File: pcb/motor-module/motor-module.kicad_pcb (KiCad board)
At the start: 2 copper layers, 37 x 27 mm, 9 parts, among them J1 Connector_male, J2 Screw_Terminal_01x02, K1 AZ822-2C-5DSE Signal-Relais, 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, Q1 2N 2222A SMD Bipolartransisto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

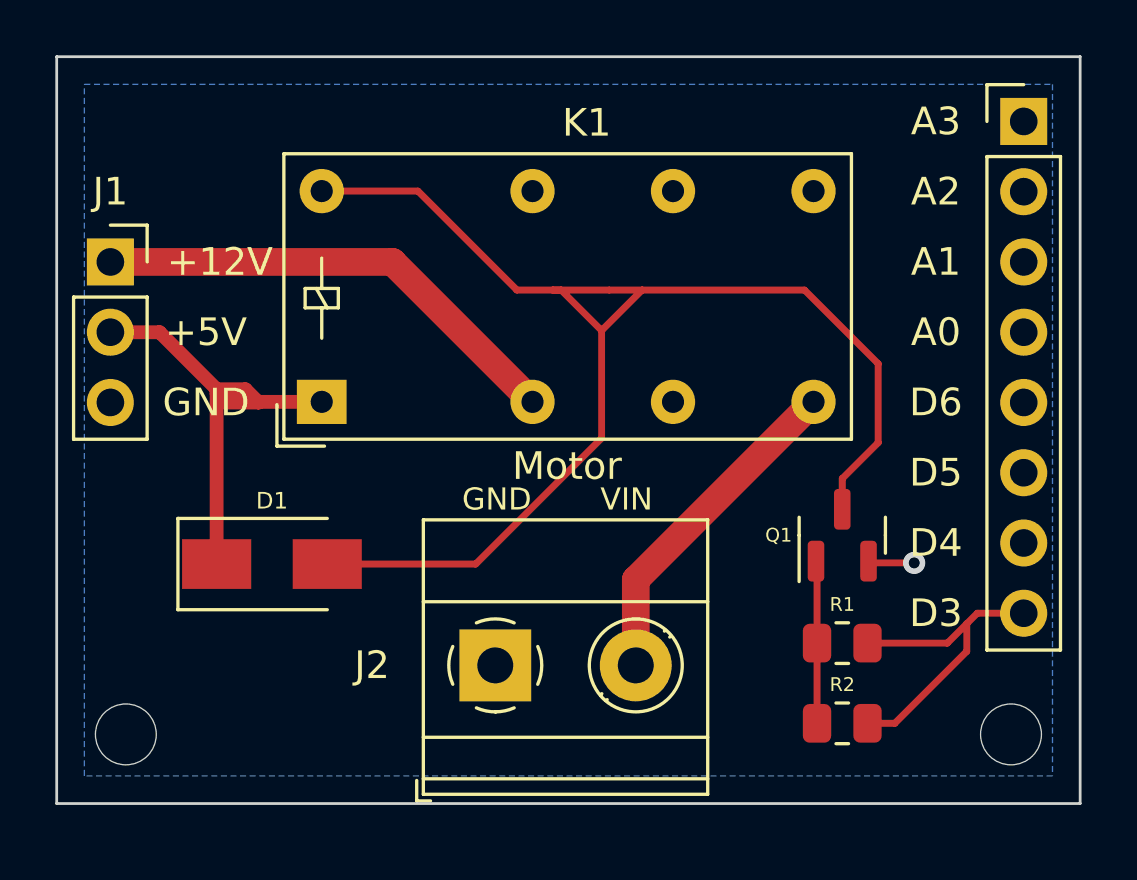
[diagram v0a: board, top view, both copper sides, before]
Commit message: added AVRISP adapter to pcb
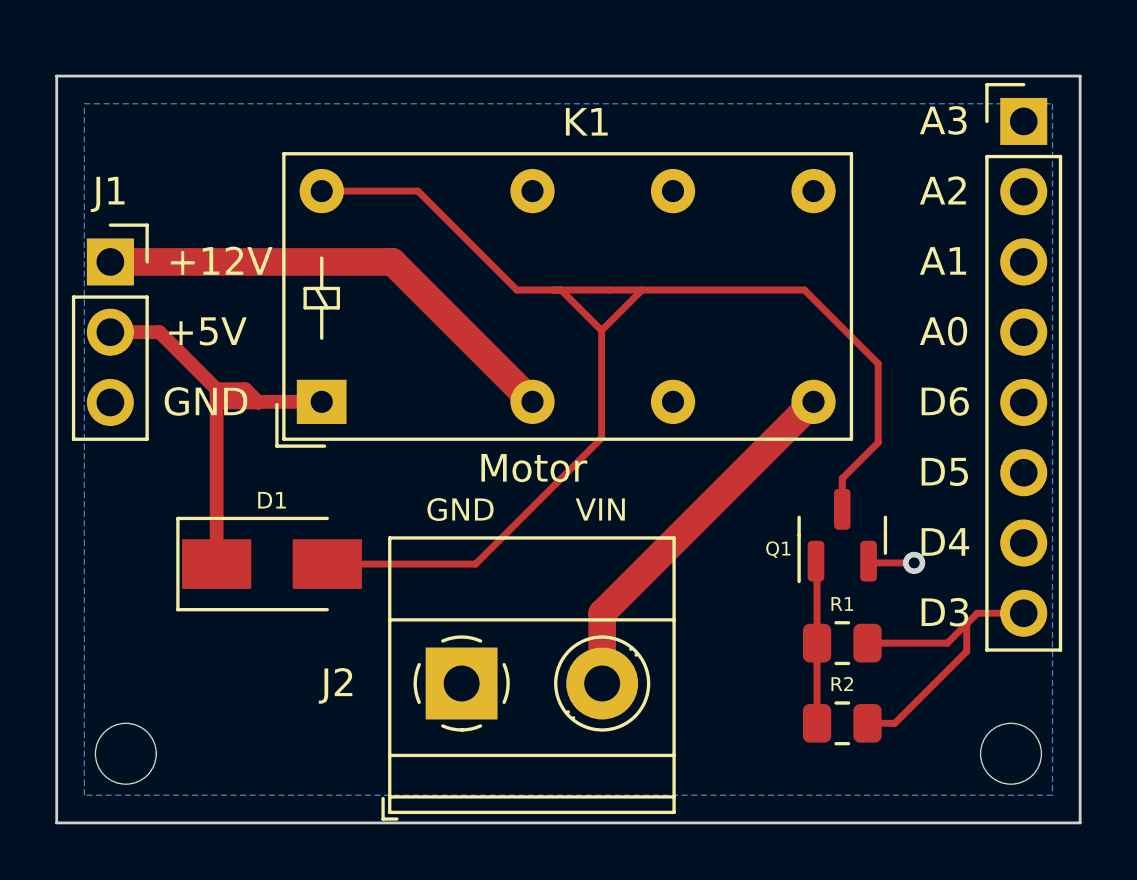
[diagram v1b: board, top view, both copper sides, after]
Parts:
- moved J2 1.38 mm to (154.9, 111.8)
- moved REF** 0.70 mm to (174.8, 114.3)
- moved REF** 0.70 mm to (142.8, 114.3)
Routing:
- net mot: track 12.2 -> 13.3 mm
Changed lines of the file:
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@@
   (net 18 "/sw-")
   (footprint "MountingHole:MountingHole_2.2mm_M2" (layer "F.Cu")
-    (at 174.8 113.6)
+    (at 174.8 114.3)
     (descr "Mounting Hole 2.2mm, no annular, M2")
     (tags "mounting hole 2.2mm no annular m2")
@@
     (property "Sheetname" "")
     (attr smd)
-    (fp_text reference "Q1" (at 0 -2.3 180) (layer "F.SilkS")
+    (fp_text reference "Q1" (at -0.5 -2.3 180) (layer "F.SilkS")
       (effects (font (size 0.5 0.5) (thickness 0.08)))
     )
@@
   )
   (footprint "MountingHole:MountingHole_2.2mm_M2" (layer "F.Cu")
-    (at 142.8 113.6)
+    (at 142.8 114.3)
     (descr "Mounting Hole 2.2mm, no annular, M2")
     (tags "mounting hole 2.2mm no annular m2")
@@
   )
   (footprint "TerminalBlock_Phoenix:TerminalBlock_Phoenix_MKDS-1,5-2-5.08_1x02_P5.08mm_Horizontal" (layer "F.Cu")
-    (at 156.155 111.105)
+    (at 154.94 111.76)
     (descr "Terminal Block Phoenix MKDS-1,5-2-5.08, 2 pins, pitch 5.08mm, size 10.2x9.8mm^2, drill diamater 1.3mm, pad diameter 2.6mm, see http://www.farnell.com/datasheets/100425.pdf, script-generated using https://github.com/pointhi/kicad-footprint-generator/scripts/TerminalBlock_Phoenix")
     (tags "THT Terminal Block Phoenix MKDS-1,5-2-5.08 pitch 5.08mm size 10.2x9.8mm^2 drill 1.3mm pad 2.6mm")
@@
       (effects (font (size 1 1) (thickness 0.15)))
     )
-    (fp_text user "A1" (at 14.605 -2.54 unlocked) (layer "F.SilkS")
+    (fp_text user "A1" (at 14.92 -2.54 unlocked) (layer "F.SilkS")
       (effects (font (size 1 1) (thickness 0.15)))
     )
@@
       (effects (font (size 1 1) (thickness 0.15)))
     )
-    (fp_text user "D3" (at 14.605 10.16 unlocked) (layer "F.SilkS")
+    (fp_text user "D3" (at 14.92 10.16 unlocked) (layer "F.SilkS")
       (effects (font (size 1 1) (thickness 0.15)))
     )
@@
       (effects (font (size 1 1) (thickness 0.15)))
     )
-    (fp_text user "D4" (at 14.605 7.62 unlocked) (layer "F.SilkS")
-      (effects (font (size 1 1) (thickness 0.15)))
-    )
-    (fp_text user "A3" (at 14.605 -7.62 unlocked) (layer "F.SilkS")
-      (effects (font (size 1 1) (thickness 0.15)))
-    )
-    (fp_text user "A0" (at 14.605 0 unlocked) (layer "F.SilkS")
-      (effects (font (size 1 1) (thickness 0.15)))
-    )
-    (fp_text user "D5" (at 14.605 5.08 unlocked) (layer "F.SilkS")
-      (effects (font (size 1 1) (thickness 0.15)))
-    )
-    (fp_text user "A2" (at 14.605 -5.08 unlocked) (layer "F.SilkS")
+    (fp_text user "D4" (at 14.92 7.62 unlocked) (layer "F.SilkS")
+      (effects (font (size 1 1) (thickness 0.15)))
+    )
+    (fp_text user "A3" (at 14.92 -7.62 unlocked) (layer "F.SilkS")
+      (effects (font (size 1 1) (thickness 0.15)))
+    )
+    (fp_text user "A0" (at 14.92 0 unlocked) (layer "F.SilkS")
+      (effects (font (size 1 1) (thickness 0.15)))
+    )
+    (fp_text user "D5" (at 14.92 5.08 unlocked) (layer "F.SilkS")
+      (effects (font (size 1 1) (thickness 0.15)))
+    )
+    (fp_text user "A2" (at 14.92 -5.08 unlocked) (layer "F.SilkS")
       (effects (font (size 1 1) (thickness 0.15)))
     )
@@
       (effects (font (size 1 1) (thickness 0.15)))
     )
-    (fp_text user "D6" (at 14.605 2.54 unlocked) (layer "F.SilkS")
+    (fp_text user "D6" (at 14.92 2.54 unlocked) (layer "F.SilkS")
       (effects (font (size 1 1) (thickness 0.15)))
     )
@@
     )
   )
-  (gr_line (start 177.3 116.1) (end 177.3 89.1) (layer "Edge.Cuts") (width 0.1))
-  (gr_line (start 140.3 116.1) (end 177.3 116.1) (layer "Edge.Cuts") (width 0.1))
-  (gr_line (start 140.3 89.1) (end 140.3 116.1) (layer "Edge.Cuts") (width 0.1))
-  (gr_line (start 177.3 89.1) (end 140.3 89.1) (layer "Edge.Cuts") (width 0.1))
-  (gr_text "Motor" (at 158.75 103.9) (layer "F.SilkS")
+  (gr_line (start 177.3 116.8) (end 177.3 89.8) (layer "Edge.Cuts") (width 0.1))
+  (gr_line (start 140.3 116.8) (end 177.3 116.8) (layer "Edge.Cuts") (width 0.1))
+  (gr_line (start 140.3 89.8) (end 140.3 116.8) (layer "Edge.Cuts") (width 0.1))
+  (gr_line (start 177.3 89.8) (end 140.3 89.8) (layer "Edge.Cuts") (width 0.1))
+  (gr_text "Motor" (at 157.5 104) (layer "F.SilkS")
     (effects (font (size 1 1) (thickness 0.15)))
   )
-  (gr_text "VIN" (at 160.9 105.1) (layer "F.SilkS")
+  (gr_text "VIN" (at 160 105.5) (layer "F.SilkS")
     (effects (font (size 0.8 0.8) (thickness 0.1)))
   )
-  (gr_text "GND" (at 156.21 105.1) (layer "F.SilkS")
+  (gr_text "GND" (at 154.9 105.5) (layer "F.SilkS")
     (effects (font (size 0.8 0.8) (thickness 0.1)))
   )
@@
   (segment (start 173.2 109.6) (end 173.58 109.22) (width 0.25) (layer "F.Cu") (net 1))
   (segment (start 173.58 109.22) (end 175.26 109.22) (width 0.25) (layer "F.Cu") (net 1))
-  (segment (start 161.235 108.005) (end 161.235 111.105) (width 1) (layer "F.Cu") (net 3))
-  (segment (start 167.6617 101.5783) (end 161.235 108.005) (width 1) (layer "F.Cu") (net 3))
+  (segment (start 160.02 109.22) (end 160.02 111.76) (width 1) (layer "F.Cu") (net 3))
+  (segment (start 167.6617 101.5783) (end 160.02 109.22) (width 1) (layer "F.Cu") (net 3))
   (segment (start 169.7125 107.4) (end 169.65 107.3375) (width 0.25) (layer "F.Cu") (net 7))
   (segment (start 171.3 107.4) (end 169.7125 107.4) (width 0.25) (layer "F.Cu") (net 7))
@@
     (polygon
       (pts
-        (xy 176.3 115.1)
-        (xy 141.3 115.1)
-        (xy 141.3 90.1)
-        (xy 176.3 90.1)
+        (xy 176.3 115.8)
+        (xy 141.3 115.8)
+        (xy 141.3 90.8)
+        (xy 176.3 90.8)
       )
     )

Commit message: m12 plug; j1939 transition
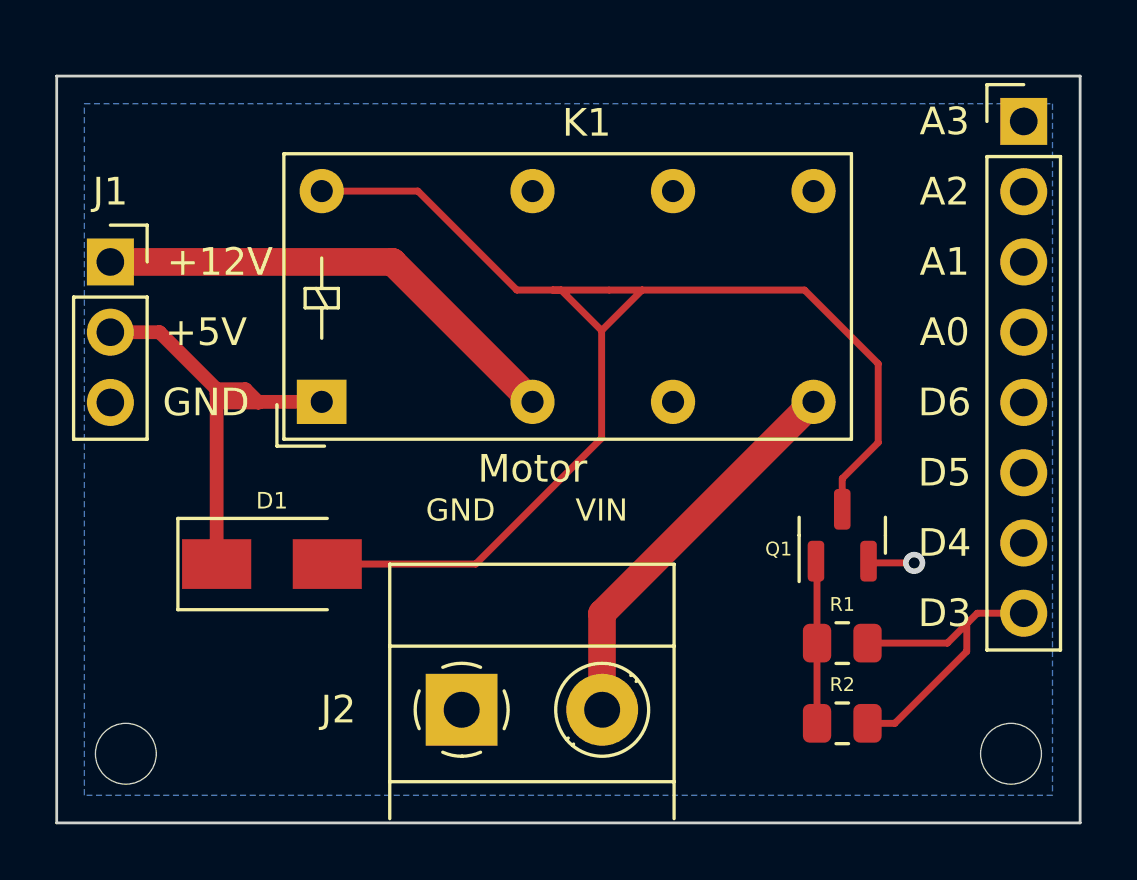
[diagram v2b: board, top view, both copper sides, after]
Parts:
- moved J2 0.95 mm to (154.9, 112.7)
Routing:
- net mot: track 13.3 -> 14.3 mm
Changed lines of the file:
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@@
   )
   (footprint "TerminalBlock_Phoenix:TerminalBlock_Phoenix_MKDS-1,5-2-5.08_1x02_P5.08mm_Horizontal" (layer "F.Cu")
-    (at 154.94 111.76)
+    (at 154.94 112.71)
     (descr "Terminal Block Phoenix MKDS-1,5-2-5.08, 2 pins, pitch 5.08mm, size 10.2x9.8mm^2, drill diamater 1.3mm, pad diameter 2.6mm, see http://www.farnell.com/datasheets/100425.pdf, script-generated using https://github.com/pointhi/kicad-footprint-generator/scripts/TerminalBlock_Phoenix")
     (tags "THT Terminal Block Phoenix MKDS-1,5-2-5.08 pitch 5.08mm size 10.2x9.8mm^2 drill 1.3mm pad 2.6mm")
@@
     )
     (fp_line (start -2.6 -5.261) (end 7.68 -5.261) (layer "F.SilkS") (width 0.12))
-    (fp_line (start -2.84 4.16) (end -2.84 4.9) (layer "F.SilkS") (width 0.12))
-    (fp_line (start -2.6 -5.261) (end -2.6 4.66) (layer "F.SilkS") (width 0.12))
+    (fp_line (start -2.6 -5.261) (end -2.6 3.937) (layer "F.SilkS") (width 0.12))
     (fp_line (start 6.355 -1.069) (end 6.308 -1.023) (layer "F.SilkS") (width 0.12))
     (fp_line (start 6.15 -1.275) (end 6.115 -1.239) (layer "F.SilkS") (width 0.12))
@@
     (fp_line (start 4.046 1.239) (end 4.011 1.274) (layer "F.SilkS") (width 0.12))
     (fp_line (start -2.6 2.6) (end 7.68 2.6) (layer "F.SilkS") (width 0.12))
-    (fp_line (start -2.6 4.1) (end 7.68 4.1) (layer "F.SilkS") (width 0.12))
-    (fp_line (start 7.68 -5.261) (end 7.68 4.66) (layer "F.SilkS") (width 0.12))
+    (fp_line (start 7.68 -5.261) (end 7.68 3.937) (layer "F.SilkS") (width 0.12))
     (fp_line (start 3.853 1.023) (end 3.806 1.069) (layer "F.SilkS") (width 0.12))
-    (fp_line (start -2.84 4.9) (end -2.34 4.9) (layer "F.SilkS") (width 0.12))
-    (fp_line (start -2.6 4.66) (end 7.68 4.66) (layer "F.SilkS") (width 0.12))
     (fp_arc (start -1.535427 0.683042) (mid -1.680501 -0.000524) (end -1.535 -0.684) (layer "F.SilkS") (width 0.12))
     (fp_arc (start -0.683042 -1.535427) (mid 0.000524 -1.680501) (end 0.684 -1.535) (layer "F.SilkS") (width 0.12))
@@
     (fp_arc (start 1.535427 -0.683042) (mid 1.680501 0.000524) (end 1.535 0.684) (layer "F.SilkS") (width 0.12))
     (fp_circle (center 5.08 0) (end 6.76 0) (layer "F.SilkS") (width 0.12) (fill none))
-    (fp_line (start 8.13 5.1) (end 8.13 -5.71) (layer "F.CrtYd") (width 0.05))
-    (fp_line (start -3.04 5.1) (end 8.13 5.1) (layer "F.CrtYd") (width 0.05))
+    (fp_line (start 8.13 4.064) (end 8.13 -5.71) (layer "F.CrtYd") (width 0.05))
+    (fp_line (start -3.04 4.064) (end 8.13 4.064) (layer "F.CrtYd") (width 0.05))
     (fp_line (start 8.13 -5.71) (end -3.04 -5.71) (layer "F.CrtYd") (width 0.05))
-    (fp_line (start -3.04 -5.71) (end -3.04 5.1) (layer "F.CrtYd") (width 0.05))
+    (fp_line (start -3.04 -5.71) (end -3.04 4.064) (layer "F.CrtYd") (width 0.05))
     (fp_line (start -2.54 2.6) (end 7.62 2.6) (layer "F.Fab") (width 0.1))
     (fp_line (start 6.035 -1.138) (end 3.943 0.955) (layer "F.Fab") (width 0.1))
-    (fp_line (start 7.62 4.6) (end -2.04 4.6) (layer "F.Fab") (width 0.1))
-    (fp_line (start -2.54 4.1) (end -2.54 -5.2) (layer "F.Fab") (width 0.1))
+    (fp_line (start -2.54 3.81) (end -2.54 -5.2) (layer "F.Fab") (width 0.1))
     (fp_line (start -2.54 -2.3) (end 7.62 -2.3) (layer "F.Fab") (width 0.1))
     (fp_line (start 6.218 -0.955) (end 4.126 1.138) (layer "F.Fab") (width 0.1))
     (fp_line (start -2.54 -5.2) (end 7.62 -5.2) (layer "F.Fab") (width 0.1))
-    (fp_line (start 7.62 -5.2) (end 7.62 4.6) (layer "F.Fab") (width 0.1))
-    (fp_line (start -2.54 4.1) (end 7.62 4.1) (layer "F.Fab") (width 0.1))
-    (fp_line (start -2.04 4.6) (end -2.54 4.1) (layer "F.Fab") (width 0.1))
+    (fp_line (start 7.62 -5.2) (end 7.62 3.81) (layer "F.Fab") (width 0.1))
     (fp_line (start 0.955 -1.138) (end -1.138 0.955) (layer "F.Fab") (width 0.1))
     (fp_line (start 1.138 -0.955) (end -0.955 1.138) (layer "F.Fab") (width 0.1))
@@
   (segment (start 173.2 109.6) (end 173.58 109.22) (width 0.25) (layer "F.Cu") (net 1))
   (segment (start 173.58 109.22) (end 175.26 109.22) (width 0.25) (layer "F.Cu") (net 1))
-  (segment (start 160.02 109.22) (end 160.02 111.76) (width 1) (layer "F.Cu") (net 3))
-  (segment (start 167.6617 101.5783) (end 160.02 109.22) (width 1) (layer "F.Cu") (net 3))
+  (segment (start 160.015 109.225) (end 160.015 112.71) (width 1) (layer "F.Cu") (net 3))
+  (segment (start 167.6617 101.5783) (end 160.015 109.225) (width 1) (layer "F.Cu") (net 3))
   (segment (start 169.7125 107.4) (end 169.65 107.3375) (width 0.25) (layer "F.Cu") (net 7))
   (segment (start 171.3 107.4) (end 169.7125 107.4) (width 0.25) (layer "F.Cu") (net 7))
@@
   (segment (start 160 99) (end 161.464 97.536) (width 0.25) (layer "F.Cu") (net 18))
   (zone (net 7) (net_name "GND") (layer "B.Cu") (hatch edge 0.508)
-    (connect_pads (clearance 0.508))
+    (connect_pads yes (clearance 0.508))
     (min_thickness 0.254) (filled_areas_thickness no)
     (fill yes (thermal_gap 0.508) (thermal_bridge_width 0.508))

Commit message: pcb update
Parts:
- removed R1, R2: 1k, Resistor_SMD:R_0805_2012Metric
- added R1_1: 1k, Resistor_SMD:R_0805_2012Metric, F.Cu at (168.7, 110.4)
- added R1_2: 1k, Resistor_SMD:R_0805_2012Metric, F.Cu at (168.7, 113.2)
- J1: value Connector_male -> Connector_male_4x8; footprint CAN_ATmega:Connector_male -> CAN_ATmega:Connector_male_4x8
- J2: value Screw_Terminal_01x02 -> Screw_Terminal_01x03; footprint TerminalBlock_Phoenix:TerminalBlock_Phoenix_MKDS-1,5-2-5.08_1x02_P5.08mm_Horizontal -> Connector_Wago:Wago_734-163_1x03_P3.50mm_Horizontal
- moved J2 4.27 mm to (155.2, 108.4)
- moved D1 2.44 mm to (145.9, 108.6)
- moved J1 1.27 mm to (158.8, 99.1)
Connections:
- J1 pad 3: GND -> unconnected-(J1-Pad3)
- J1 pad 4: CMD -> GND
- J1 pad 5: unconnected-(J1-Pad5) -> CMD
- J2 pad 1: GND -> mot
- J2 pad 2: mot -> unconnected-(J2-Pad2)
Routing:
- net /sw-: track 48.6 -> 45.1 mm
- net +5V: track 16.7 -> 20.1 mm
- net CMD: track 11.8 -> 8.95 mm
- net mot: track 14.3 -> 16.4 mm
- net +12V: track 17.4 -> 18.4 mm
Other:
- board text removed: "GND"
- board text removed: "Motor"
- board text removed: "VIN"
